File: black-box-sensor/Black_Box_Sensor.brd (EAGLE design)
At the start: 37.2 x 44 mm, 56 parts, among them J1 104031-0811, J2 UX60-MB-5S8, J3 B4B-PH-SM4-TBT(LF)(SN), U1 ADXL375, U2 ADXL375, U3 ATMEGA32U4-AU, U4 FXAS21002CQR1, U5 MIC5504-3.3YM5-TR, U6 NL27WZ32USG, U7 LT1129CST-5#PBF, U8 AD8426ACPZ-WP, U9 TXU0304

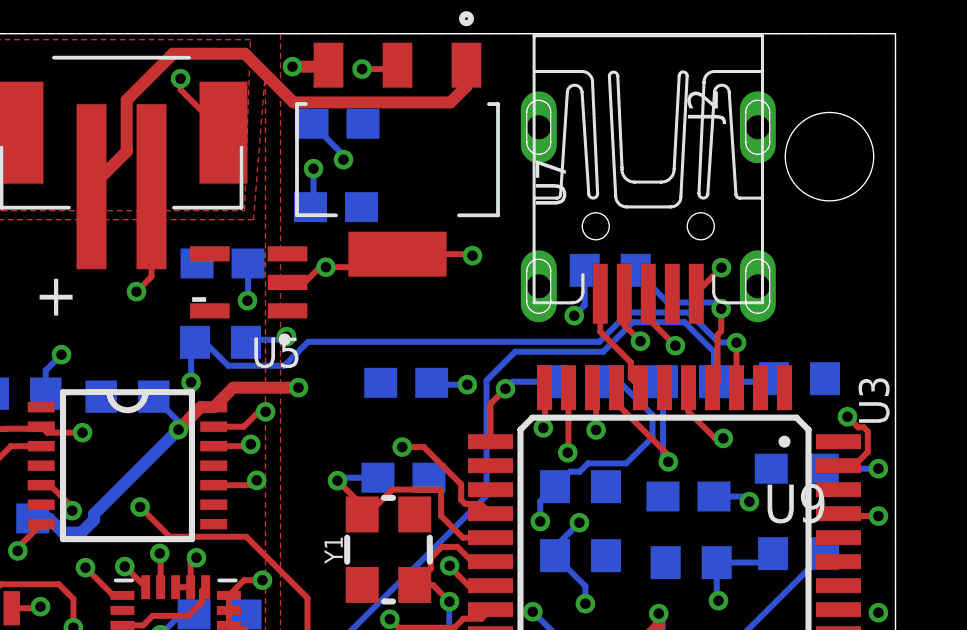
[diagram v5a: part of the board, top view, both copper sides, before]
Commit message: move resistors
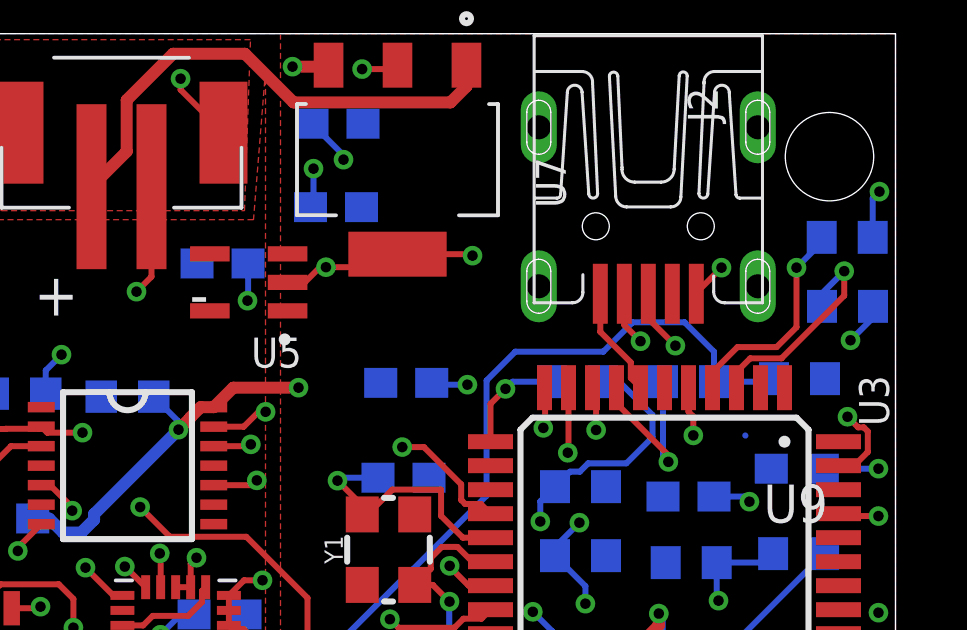
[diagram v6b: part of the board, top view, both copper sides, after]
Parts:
- moved R1 20.9 mm to (35.6, 34.9)
- moved R2 7.98 mm to (35.6, 37.2), turned to 180 degrees
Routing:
- net D-: track 22.4 -> 8.59 mm, vias 2 -> 1
- net N$2: track 7.94 -> 14.5 mm
- net N$3: track 15.1 -> 11.0 mm
- net D+: track 6.14 -> 7.28 mm
- net GND: track 77.1 -> 76.4 mm
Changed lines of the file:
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@@
 <attribute name="VALUE" x="21.525" y="30.455" size="1.27" layer="28" rot="MR0"/>
 </element>
-<element name="R1" library="rcl" library_urn="urn:adsk.eagle:library:334" package="R0603" package3d_urn="urn:adsk.eagle:package:23555/3" value="22" x="14.7" y="33.71" smashed="yes" rot="MR180">
-<attribute name="NAME" x="32.565" y="36.475" size="1.27" layer="26" rot="MR180"/>
-<attribute name="POPULARITY" value="77" x="14.7" y="33.71" size="1.778" layer="28" rot="MR180" display="off"/>
-<attribute name="SPICEPREFIX" value="R" x="14.7" y="33.71" size="1.778" layer="28" rot="MR180" display="off"/>
-<attribute name="VALUE" x="14.065" y="35.615" size="1.27" layer="28" rot="MR180"/>
-</element>
-<element name="R2" library="rcl" library_urn="urn:adsk.eagle:library:334" package="R0603" package3d_urn="urn:adsk.eagle:package:23555/3" value="22" x="27.69" y="36.11" smashed="yes" rot="MR0">
-<attribute name="NAME" x="28.325" y="37.145" size="1.27" layer="26" rot="MR0"/>
-<attribute name="POPULARITY" value="77" x="27.69" y="36.11" size="1.778" layer="28" rot="MR0" display="off"/>
-<attribute name="SPICEPREFIX" value="R" x="27.69" y="36.11" size="1.778" layer="28" rot="MR0" display="off"/>
-<attribute name="VALUE" x="28.325" y="34.205" size="1.27" layer="28" rot="MR0"/>
+<element name="R1" library="rcl" library_urn="urn:adsk.eagle:library:334" package="R0603" package3d_urn="urn:adsk.eagle:package:23555/3" value="22" x="35.6" y="34.91" smashed="yes" rot="MR180">
+<attribute name="NAME" x="53.465" y="37.675" size="1.27" layer="26" rot="MR180"/>
+<attribute name="POPULARITY" value="77" x="35.6" y="34.91" size="1.778" layer="28" rot="MR180" display="off"/>
+<attribute name="SPICEPREFIX" value="R" x="35.6" y="34.91" size="1.778" layer="28" rot="MR180" display="off"/>
+<attribute name="VALUE" x="34.965" y="36.815" size="1.27" layer="28" rot="MR180"/>
+</element>
+<element name="R2" library="rcl" library_urn="urn:adsk.eagle:library:334" package="R0603" package3d_urn="urn:adsk.eagle:package:23555/3" value="22" x="35.59" y="37.21" smashed="yes" rot="MR180">
+<attribute name="NAME" x="34.955" y="36.175" size="1.27" layer="26" rot="MR180"/>
+<attribute name="POPULARITY" value="77" x="35.59" y="37.21" size="1.778" layer="28" rot="MR180" display="off"/>
+<attribute name="SPICEPREFIX" value="R" x="35.59" y="37.21" size="1.778" layer="28" rot="MR180" display="off"/>
+<attribute name="VALUE" x="34.955" y="39.115" size="1.27" layer="28" rot="MR180"/>
 </element>
 <element name="C17" library="rcl" library_urn="urn:adsk.eagle:library:334" package="C0603" package3d_urn="urn:adsk.eagle:package:23616/2" value="0.1uF" x="11.89" y="14.29" smashed="yes" rot="MR180">
@@
 <wire x1="30.56" y1="35.33" x2="30.56" y2="35.36" width="0.2" layer="1"/>
 <via x="31.4" y="36.2" extent="1-16" drill="0.35"/>
-<wire x1="31.46" y1="30.51" x2="31.19" y2="30.51" width="0.2" layer="1"/>
-<wire x1="31.19" y1="30.51" x2="30.3" y2="31.4" width="0.2" layer="1"/>
+<wire x1="30.46" y1="30.61" x2="30.46" y2="31.24" width="0.2" layer="1"/>
+<wire x1="30.46" y1="31.24" x2="30.3" y2="31.4" width="0.2" layer="1"/>
 <wire x1="30.3" y1="32.2" x2="30.3" y2="31.4" width="0.2" layer="1"/>
-<via x="31.46" y="30.51" extent="1-16" drill="0.35"/>
+<via x="30.46" y="30.61" extent="1-16" drill="0.35"/>
 <wire x1="12.4" y1="38.9" x2="12.4" y2="35.9" width="0.2" layer="1"/>
 <wire x1="12.4" y1="35.9" x2="11.9" y2="35.4" width="0.2" layer="1"/>
@@
 <contactref element="U3" pad="3"/>
 <contactref element="R1" pad="1"/>
-<via x="13.72" y="32.38" extent="1-16" drill="0.35"/>
-<wire x1="13.72" y1="32.38" x2="13.72" y2="33.58" width="0.2" layer="16"/>
-<wire x1="13.72" y1="33.58" x2="13.85" y2="33.71" width="0.2" layer="16"/>
-<wire x1="31.89" y1="33.71" x2="31.9" y2="33.7" width="0.2" layer="16"/>
-<via x="31.9" y="33.7" extent="1-16" drill="0.35"/>
-<wire x1="27.32414375" y1="33.727" x2="28.30334375" y2="34.7062" width="0.2" layer="16"/>
-<wire x1="31.30245" y1="33.71" x2="31.89" y2="33.71" width="0.2" layer="16"/>
-<wire x1="28.30334375" y1="34.7062" x2="30.30625" y2="34.7062" width="0.2" layer="16"/>
-<wire x1="30.30625" y1="34.7062" x2="31.30245" y2="33.71" width="0.2" layer="16"/>
-<wire x1="13.85" y1="33.71" x2="14.178975" y2="33.71" width="0.2" layer="16"/>
-<wire x1="14.178975" y1="33.71" x2="14.955975" y2="32.933" width="0.2" layer="16"/>
-<wire x1="14.955975" y1="32.933" x2="16.82480625" y2="32.933" width="0.2" layer="16"/>
-<wire x1="16.82480625" y1="32.933" x2="17.61880625" y2="33.727" width="0.2" layer="16"/>
-<wire x1="17.61880625" y1="33.727" x2="27.32414375" y2="33.727" width="0.2" layer="16"/>
-<wire x1="31.9" y1="33.7" x2="31.9" y2="32.2" width="0.2" layer="1"/>
+<wire x1="32.19" y1="30.61" x2="32.2" y2="30.6" width="0.2" layer="16"/>
+<wire x1="34.75" y1="34.91" x2="35.078975" y2="34.91" width="0.2" layer="16"/>
+<wire x1="34.75" y1="34.91" x2="34.533875" y2="35.126125" width="0.2" layer="16"/>
+<wire x1="34.533875" y1="35.126125" x2="35.4914" y2="36.08365" width="0.2" layer="16"/>
+<via x="35.4914" y="36.08365" extent="1-16" drill="0.35"/>
+<wire x1="31.9" y1="32.2" x2="31.9" y2="32.80044375" width="0.2" layer="1"/>
+<wire x1="31.9" y1="32.2" x2="31.9" y2="32.721025" width="0.2" layer="1"/>
+<wire x1="31.9" y1="32.721025" x2="32.355975" y2="33.177" width="0.2" layer="1"/>
+<wire x1="32.355975" y1="33.177" x2="33.4" y2="33.177" width="0.2" layer="1"/>
+<wire x1="33.4" y1="33.177" x2="35.4914" y2="35.2684" width="0.2" layer="1"/>
+<wire x1="35.4914" y1="35.2684" x2="35.4914" y2="36.08365" width="0.2" layer="1"/>
+<wire x1="31.9" y1="32.2" x2="32.19" y2="30.61" width="0" layer="19" extent="1-16"/>
 </signal>
 <signal name="D+">
 <contactref element="U3" pad="4"/>
 <contactref element="R2" pad="1"/>
-<wire x1="28.54" y1="36.11" x2="29.61415" y2="35.03585" width="0.2" layer="16"/>
-<wire x1="31.1914" y1="35.03585" x2="31.3914" y2="34.83585" width="0.2" layer="16"/>
-<wire x1="31.1914" y1="35.03585" x2="29.61415" y2="35.03585" width="0.2" layer="16"/>
-<via x="31.3914" y="34.83585" extent="1-16" drill="0.35"/>
-<wire x1="31.3914" y1="34.83585" x2="31.3914" y2="34.08320625" width="0.2" layer="1"/>
-<wire x1="31.3914" y1="34.08320625" x2="31.2694" y2="33.96120625" width="0.2" layer="1"/>
-<wire x1="31.2694" y1="33.96120625" x2="31.2694" y2="32.3694" width="0.2" layer="1"/>
-<wire x1="31.2694" y1="32.3694" x2="31.1" y2="32.2" width="0.2" layer="1"/>
+<wire x1="34.74" y1="37.21" x2="34.74" y2="37.04" width="0.2" layer="16"/>
+<wire x1="34.74" y1="37.04" x2="33.9" y2="36.2" width="0.2" layer="16"/>
+<via x="33.9" y="36.2" extent="1-16" drill="0.35"/>
+<wire x1="33.237" y1="33.553" x2="31.931975" y2="33.553" width="0.2" layer="1"/>
+<wire x1="31.931975" y1="33.553" x2="31.1" y2="32.721025" width="0.2" layer="1"/>
+<wire x1="31.1" y1="32.721025" x2="31.1" y2="32.2" width="0.2" layer="1"/>
+<wire x1="33.9" y1="36.2" x2="33.9" y2="34.216" width="0.2" layer="1"/>
+<wire x1="33.9" y1="34.216" x2="33.237" y2="33.553" width="0.2" layer="1"/>
 </signal>
 <signal name="VBUS">
@@
 <contactref element="J2" pad="3"/>
 <contactref element="R2" pad="2"/>
-<wire x1="26.84" y1="36.11" x2="26.84" y2="34.9486" width="0.2" layer="16"/>
-<wire x1="26.84" y1="34.9486" x2="26.4914" y2="34.6" width="0.2" layer="16"/>
-<via x="26.4914" y="34.6" extent="1-16" drill="0.35"/>
 <via x="29.8628" y="33.6" extent="1-16" drill="0.35"/>
-<wire x1="29.44320625" y1="33.6" x2="29.8628" y2="33.6" width="0.2" layer="15"/>
-<wire x1="28.96120625" y1="33.118" x2="29.44320625" y2="33.6" width="0.2" layer="15"/>
-<wire x1="26.4914" y1="34.6" x2="27.9734" y2="33.118" width="0.2" layer="15"/>
-<wire x1="27.9734" y1="33.118" x2="28.96120625" y2="33.118" width="0.2" layer="15"/>
 <wire x1="29.8628" y1="33.6" x2="28.96" y2="34.5028" width="0.2" layer="1"/>
 <wire x1="28.96" y1="34.5028" x2="28.96" y2="35.33" width="0.2" layer="1"/>
+<wire x1="36.44" y1="37.21" x2="36.44" y2="38.51071875" width="0.2" layer="16"/>
+<wire x1="36.44" y1="38.51071875" x2="36.664640625" y2="38.735359375" width="0.2" layer="16"/>
+<via x="36.664640625" y="38.735359375" extent="1-16" drill="0.35"/>
+<wire x1="29.8628" y1="33.6" x2="30.0098" y2="33.453" width="0.2" layer="2"/>
+<wire x1="36.664640625" y1="35.840915625" x2="34.276728125" y2="33.453" width="0.2" layer="2"/>
+<wire x1="34.276728125" y1="33.453" x2="30.0098" y2="33.453" width="0.2" layer="2"/>
+<wire x1="36.664640625" y1="35.840915625" x2="36.664640625" y2="38.735359375" width="0.2" layer="2"/>
 </signal>
 <signal name="N$3">
 <contactref element="R1" pad="2"/>
 <contactref element="J2" pad="4"/>
-<via x="16.9" y="33.9" extent="1-16" drill="0.35"/>
-<wire x1="16.9" y1="33.9" x2="16.8" y2="33.9" width="0.2" layer="16"/>
-<wire x1="16.8" y1="33.9" x2="16.7" y2="33.8" width="0.2" layer="16"/>
-<wire x1="16.7" y1="33.8" x2="15.64" y2="33.8" width="0.2" layer="16"/>
-<wire x1="15.64" y1="33.8" x2="15.55" y2="33.71" width="0.2" layer="16"/>
+<wire x1="36.54" y1="35" x2="36.45" y2="34.91" width="0.2" layer="16"/>
 <wire x1="28.16" y1="35.33" x2="28.16" y2="34.2886" width="0.2" layer="1"/>
 <wire x1="28.16" y1="34.2886" x2="28.7" y2="33.7486" width="0.2" layer="1"/>
 <via x="28.7" y="33.7486" extent="1-16" drill="0.35"/>
-<wire x1="28.7" y1="33.7486" x2="17.0514" y2="33.7486" width="0.2" layer="2"/>
-<wire x1="17.0514" y1="33.7486" x2="16.9" y2="33.9" width="0.2" layer="2"/>
+<wire x1="36.45" y1="34.91" x2="36.45" y2="34.53" width="0.2" layer="16"/>
+<wire x1="36.45" y1="34.53" x2="35.7" y2="33.78" width="0.2" layer="16"/>
+<via x="35.7" y="33.78" extent="1-16" drill="0.35"/>
+<wire x1="28.7" y1="33.7486" x2="28.82239375" y2="33.7486" width="0.2" layer="2"/>
+<wire x1="28.82239375" y1="33.7486" x2="29.60159375" y2="32.9694" width="0.2" layer="2"/>
+<wire x1="29.60159375" y1="32.9694" x2="34.8894" y2="32.9694" width="0.2" layer="2"/>
+<wire x1="34.8894" y1="32.9694" x2="35.7" y2="33.78" width="0.2" layer="2"/>
 </signal>
 <signal name="N$5">

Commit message: place and connect new 3v3
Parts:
- removed U5: MIC5504-3.3YM5-TR, BBS_Library:SOT-23-5_MC_MCH
- added U$1: XC6222B331MR-G, BBS_Library:SOT-25
- moved C1 4.40 mm to (20.9, 34.5)
- moved C2 1.49 mm to (15.6, 35.1), turned to 180 degrees
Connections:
- net +5V: now also U$1.1, U$1.3; no longer U5.1, U5.3
- net 3.3V: now also U$1.5; no longer U5.5
- net GND: now also U$1.2; no longer U5.2
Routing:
- net N$2: track 14.5 -> 11.4 mm

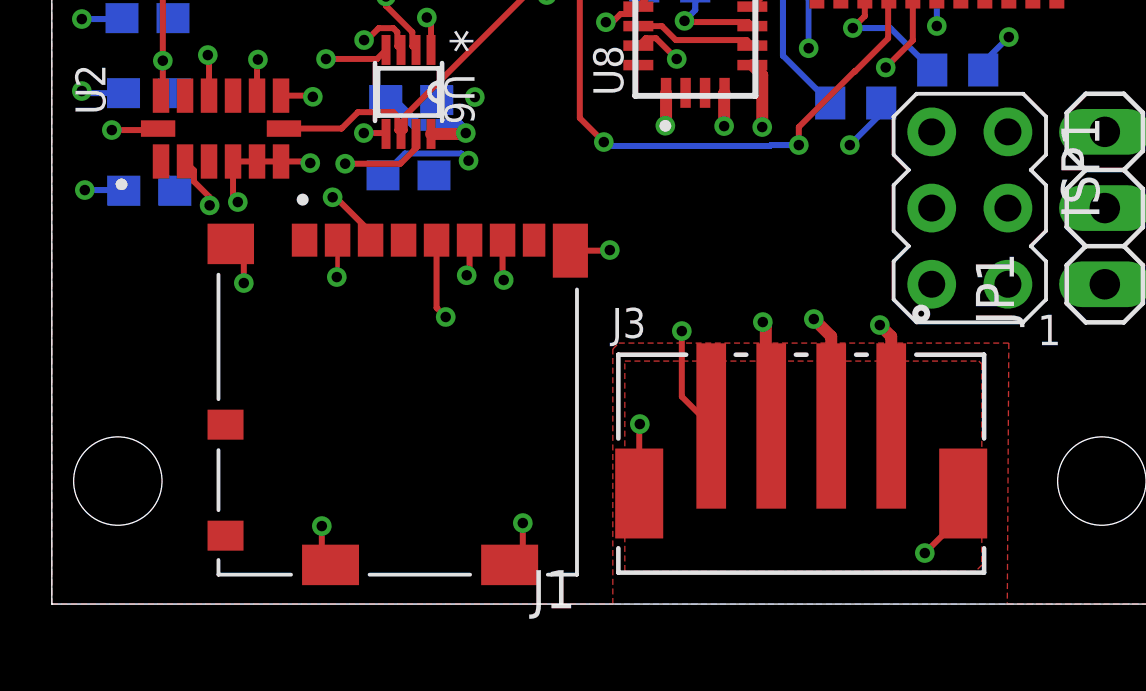
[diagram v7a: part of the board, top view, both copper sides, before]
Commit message: add orientation of SD card reader to silkscreen; update orientation to reflect
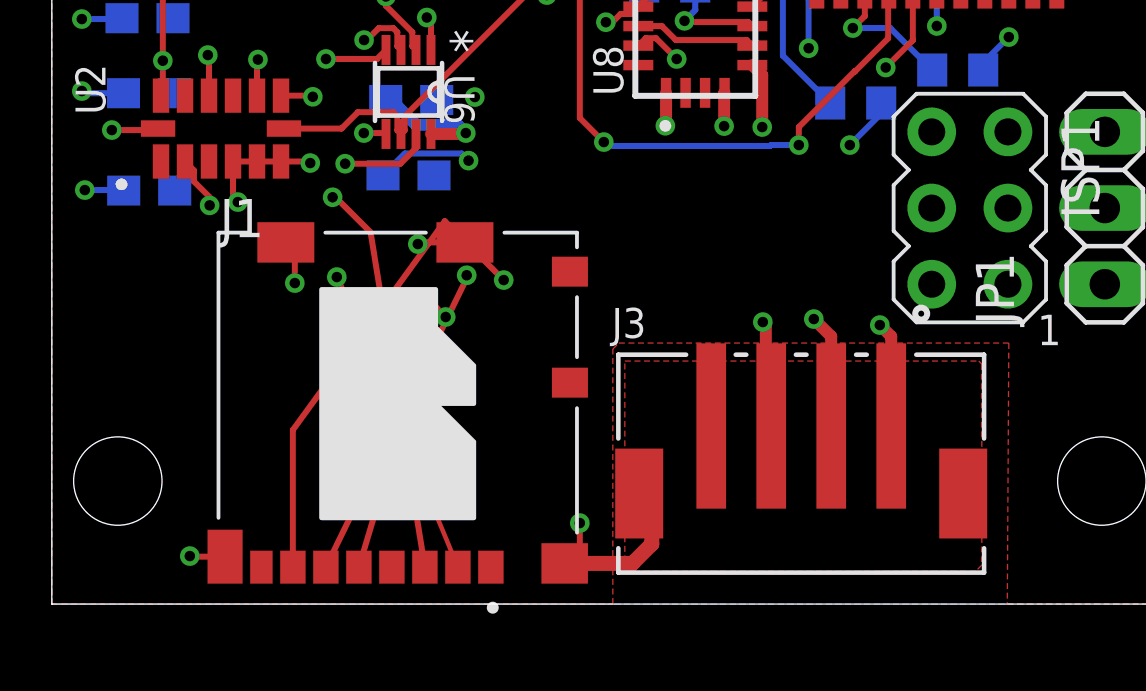
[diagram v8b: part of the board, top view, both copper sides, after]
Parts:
- turned J1 to 0 degrees
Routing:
- net MISO: track 41.8 -> 56.4 mm
- net MOSI: track 23.5 -> 34.6 mm
- net CS4: track 35.7 -> 45.0 mm
- net GND: track 76.3 -> 83.9 mm, vias 34 -> 31
- net SCLK: track 46.3 -> 53.0 mm
